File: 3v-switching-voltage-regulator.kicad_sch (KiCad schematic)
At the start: 16 parts, among them J1 USB_C_Receptacle_PowerOnly_6P, U1 MP1584EN

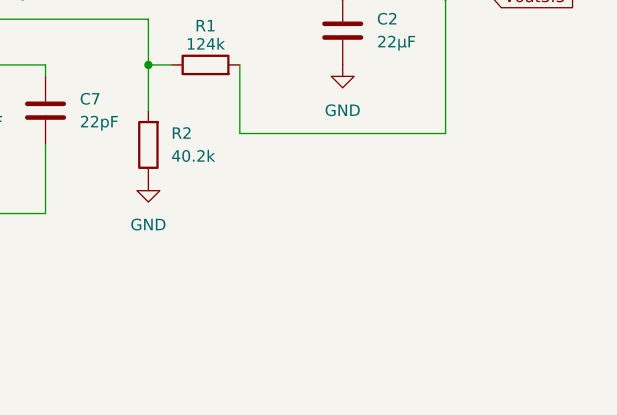
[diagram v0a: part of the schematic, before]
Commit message: reduces board size and adds input output connections
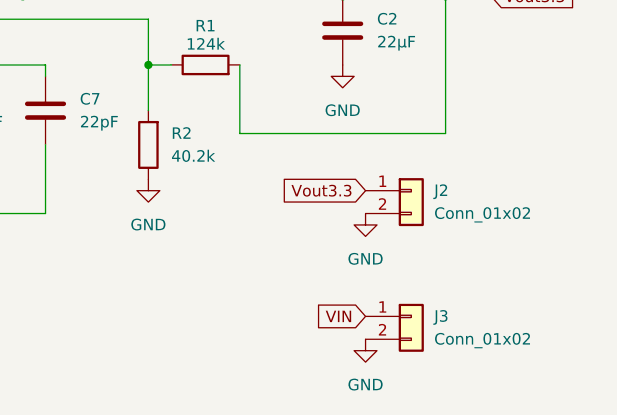
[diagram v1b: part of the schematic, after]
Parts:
- added J2, J3: Conn_01x02, Connector_PinHeader_2.54mm:PinHeader_1x02_P2.54mm_Vertical, symbol Connector_Generic:Conn_01x02
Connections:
- net GND: now also J2.2 (Pin_2), J3.2 (Pin_2)
- net VIN: now also J3.1 (Pin_1)
- net Vout3.3: now also J2.1 (Pin_1)
